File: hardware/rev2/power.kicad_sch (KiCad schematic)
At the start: 19 parts, among them J8 Battery Connection, U5 MP2664GG-xxxx-P, U6 MAX17055ETB+, U8 TPS631000DRLR

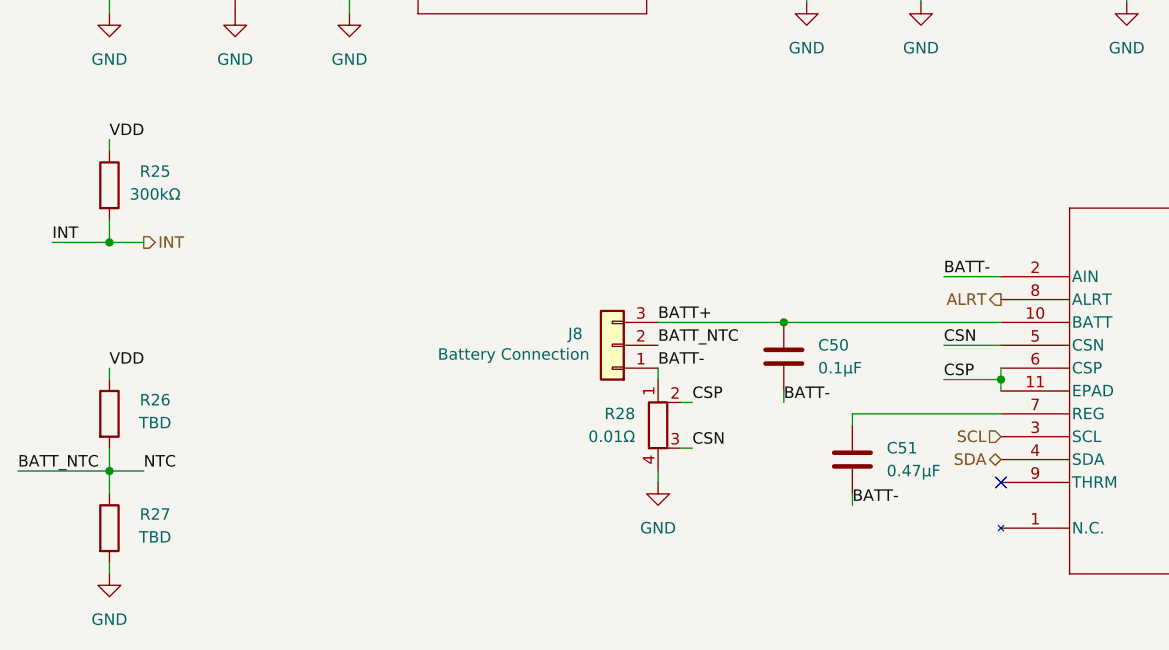
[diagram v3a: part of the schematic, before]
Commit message: Started power system layout
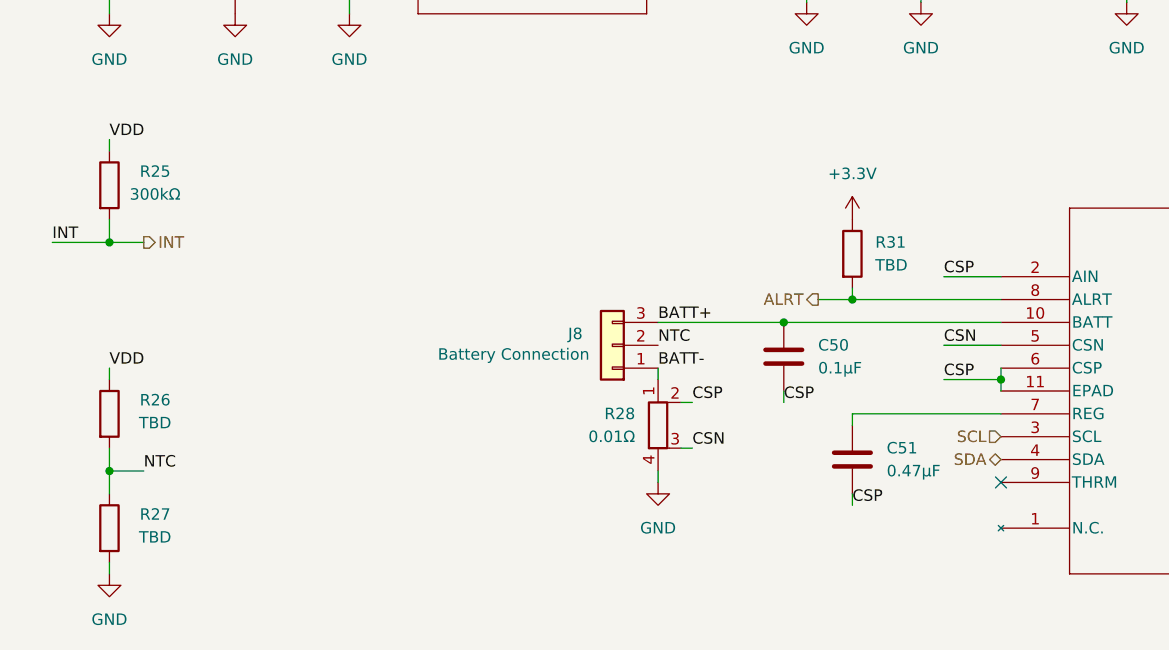
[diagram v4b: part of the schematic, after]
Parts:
- added R31: TBD, Resistor_SMD:R_0603_1608Metric_Pad0.98x0.95mm_HandSolder, symbol Device:R
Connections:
- net +3.3V: now also R31.1
- net ALRT: now also R31.2
- net BATT-: no longer C50.2, C51.2, U6.2 (AIN)
- net CSP: now also C50.2, C51.2, U6.2 (AIN)
- net BATT_NTC renamed NTC
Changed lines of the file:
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@@
 	)
 	(junction
+		(at 120.65 121.92)
+		(diameter 0)
+		(color 0 0 0 0)
+	)
+	(junction
 		(at 38.1 74.93)
 		(diameter 0)
@@
 	(wire
 		(pts
+			(xy 116.84 121.92) (xy 120.65 121.92)
+		)
+		(stroke
+			(width 0)
+			(type default)
+		)
+	)
+	(wire
+		(pts
 			(xy 38.1 143.51) (xy 38.1 140.97)
 		)
@@
 	(wire
 		(pts
-			(xy 113.03 133.35) (xy 113.03 132.08)
+			(xy 120.65 121.92) (xy 137.16 121.92)
 		)
 		(stroke
@@
 	(wire
 		(pts
-			(xy 156.21 72.39) (xy 162.56 72.39)
+			(xy 113.03 133.35) (xy 113.03 132.08)
 		)
 		(stroke
@@
 	(wire
 		(pts
-			(xy 130.81 127) (xy 137.16 127)
+			(xy 156.21 72.39) (xy 162.56 72.39)
 		)
 		(stroke
@@
 	(wire
 		(pts
-			(xy 128.27 74.93) (xy 151.13 74.93)
+			(xy 130.81 127) (xy 137.16 127)
 		)
 		(stroke
@@
 	(wire
 		(pts
-			(xy 38.1 140.97) (xy 41.91 140.97)
+			(xy 128.27 74.93) (xy 151.13 74.93)
 		)
 		(stroke
@@
 	(wire
 		(pts
-			(xy 27.94 140.97) (xy 38.1 140.97)
+			(xy 38.1 140.97) (xy 41.91 140.97)
 		)
 		(stroke
@@
 	(wire
 		(pts
+			(xy 120.65 120.65) (xy 120.65 121.92)
+		)
+		(stroke
+			(width 0)
+			(type default)
+		)
+	)
+	(wire
+		(pts
 			(xy 199.39 53.34) (xy 162.56 53.34)
 		)
@@
 		)
 	)
-	(label "BATT-"
+	(label "CSP"
 		(at 120.65 144.78 0)
 		(effects
@@
 		)
 	)
-	(label "BATT_NTC"
-		(at 27.94 140.97 0)
-		(effects
-			(font
-				(size 1.27 1.27)
-			)
-			(justify left bottom)
-		)
-	)
 	(label "BATT-"
 		(at 99.06 129.54 0)
@@
 		)
 	)
-	(label "BATT-"
+	(label "CSP"
 		(at 113.03 133.35 0)
 		(effects
@@
 		)
 	)
-	(label "BATT_NTC"
+	(label "NTC"
 		(at 99.06 127 0)
 		(effects
@@
 		)
 	)
-	(label "BATT-"
+	(label "CSP"
 		(at 130.81 119.38 0)
 		(effects
@@
 	(hierarchical_label "ALRT"
 		(shape output)
-		(at 137.16 121.92 180)
+		(at 116.84 121.92 180)
 		(effects
 			(font
@@
 	)
 	(symbol
+		(lib_id "power:+3.3V")
+		(at 120.65 113.03 0)
+		(unit 1)
+		(body_style 1)
+		(exclude_from_sim no)
+		(in_bom yes)
+		(on_board yes)
+		(in_pos_files yes)
+		(dnp no)
+		(fields_autoplaced yes)
+		(property "Reference" "#PWR087"
+			(at 120.65 116.84 0)
+			(hide yes)
+			(show_name no)
+			(do_not_autoplace no)
+			(effects
+				(font
+					(size 1.27 1.27)
+				)
+			)
+		)
+		(property "Value" "+3.3V"
+			(at 120.65 107.95 0)
+			(show_name no)
+			(do_not_autoplace no)
+			(effects
+				(font
+					(size 1.27 1.27)
+				)
+			)
+		)
+		(property "Footprint" ""
+			(at 120.65 113.03 0)
+			(hide yes)
+			(show_name no)
+			(do_not_autoplace no)
+			(effects
+				(font
+					(size 1.27 1.27)
+				)
+			)
+		)
+		(property "Datasheet" ""
+			(at 120.65 113.03 0)
+			(hide yes)
+			(show_name no)
+			(do_not_autoplace no)
+			(effects
+				(font
+					(size 1.27 1.27)
+				)
+			)
+		)
+		(property "Description" "Power symbol creates a global label with name \"+3.3V\""
+			(at 120.65 113.03 0)
+			(hide yes)
+			(show_name no)
+			(do_not_autoplace no)
+			(effects
+				(font
+					(size 1.27 1.27)
+				)
+			)
+		)
+		(pin "1"
+		)
+		(instances
+			(project "rev2"
+				(path "/9067f306-e23c-4d77-8182-4fa2c4b88902/46484475-7656-401a-9d45-159f5e421427"
+					(reference "#PWR087")
+					(unit 1)
+				)
+			)
+		)
+	)
+	(symbol
 		(lib_id "power:GND")
 		(at 64.77 90.17 0)
@@
 					(unit 1)
 				)
+			)
+		)
+	)
+	(symbol
+		(lib_id "Device:R")
+		(at 120.65 116.84 0)
+		(unit 1)
+		(body_style 1)
+		(exclude_from_sim no)
+		(in_bom yes)
+		(on_board yes)
+		(in_pos_files yes)
+		(dnp no)
+		(property "Reference" "R31"
+			(at 123.19 115.5699 0)
+			(show_name no)
+			(do_not_autoplace no)
+			(effects
+				(font
+					(size 1.27 1.27)
+				)
+				(justify left)
+			)
+		)
+		(property "Value" "TBD"
+			(at 123.19 118.11 0)
+			(show_name no)
+			(do_not_autoplace no)
+			(effects
+				(font
+					(size 1.27 1.27)
+				)
+				(justify left)
+			)
+		)
+		(property "Footprint" "Resistor_SMD:R_0603_1608Metric_Pad0.98x0.95mm_HandSolder"
+			(at 118.872 116.84 90)
+			(hide yes)
+			(show_name no)
+			(do_not_autoplace no)
+			(effects
+				(font
+					(size 1.27 1.27)
+				)
+			)
+		)
+		(property "Datasheet" ""
+			(at 120.65 116.84 0)
+			(hide yes)
+			(show_name no)
+			(do_not_autoplace no)
+			(effects
+				(font
+					(size 1.27 1.27)
+				)
+			)
+		)
+		(property "Description" "Resistor"
+			(at 120.65 116.84 0)
+			(hide yes)
+			(show_name no)
+			(do_not_autoplace no)
+			(effects
+				(font
+					(size 1.27 1.27)
+				)
+			)
+		)
+		(pin "1"
+		)
+		(pin "2"
+		)
+		(instances
+			(project "rev2"
+				(path "/9067f306-e23c-4d77-8182-4fa2c4b88902/46484475-7656-401a-9d45-159f5e421427"
+					(reference "R31")
+					(unit 1)
+				)

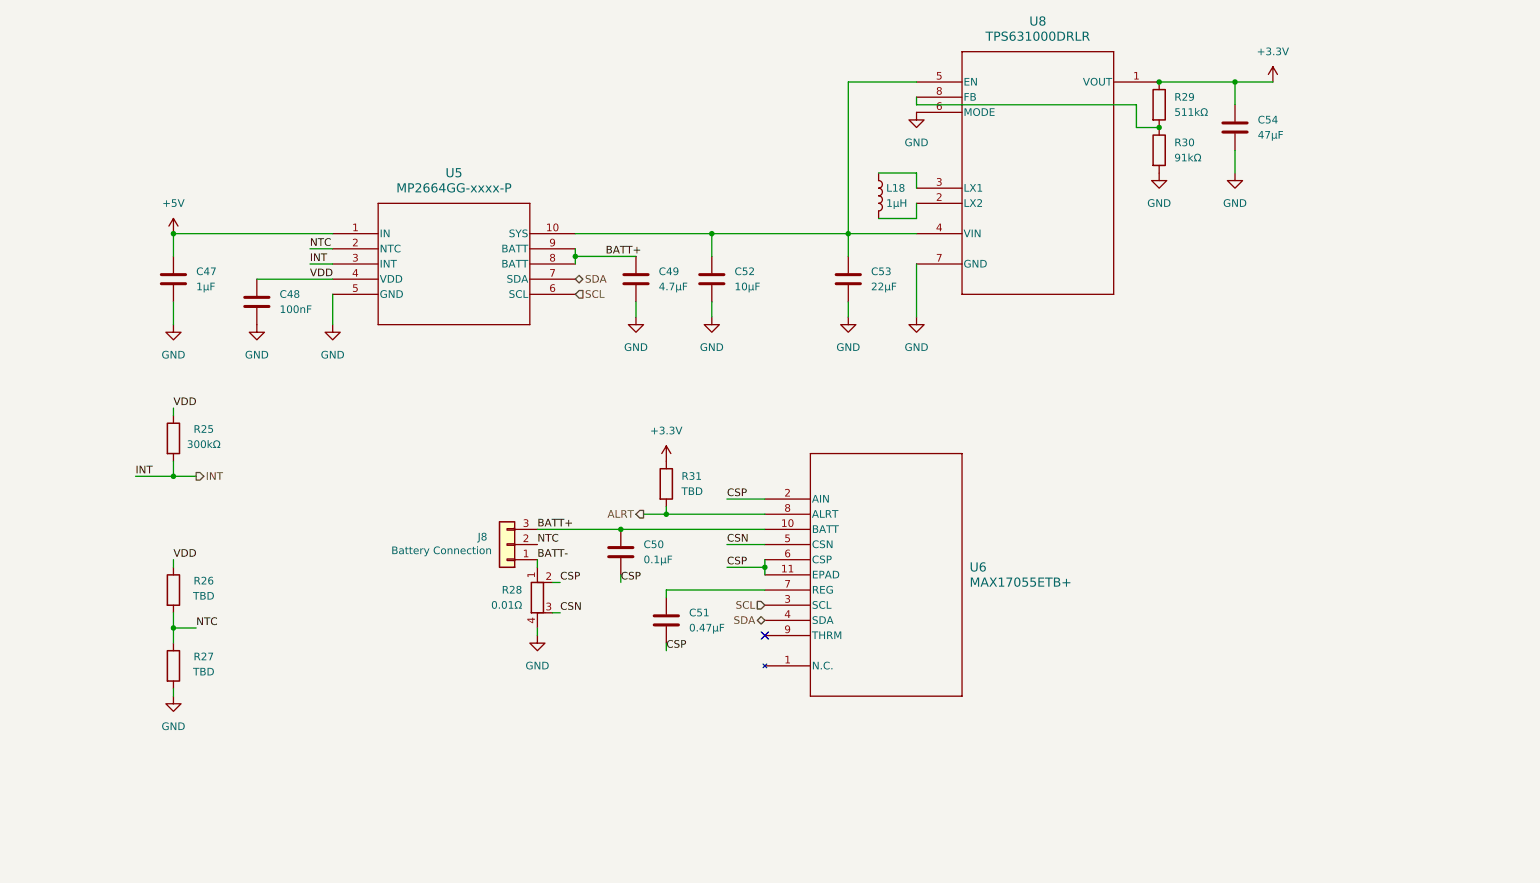
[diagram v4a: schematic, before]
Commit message: added testpoints, added LEDs, fixed a lot of DRC stuff
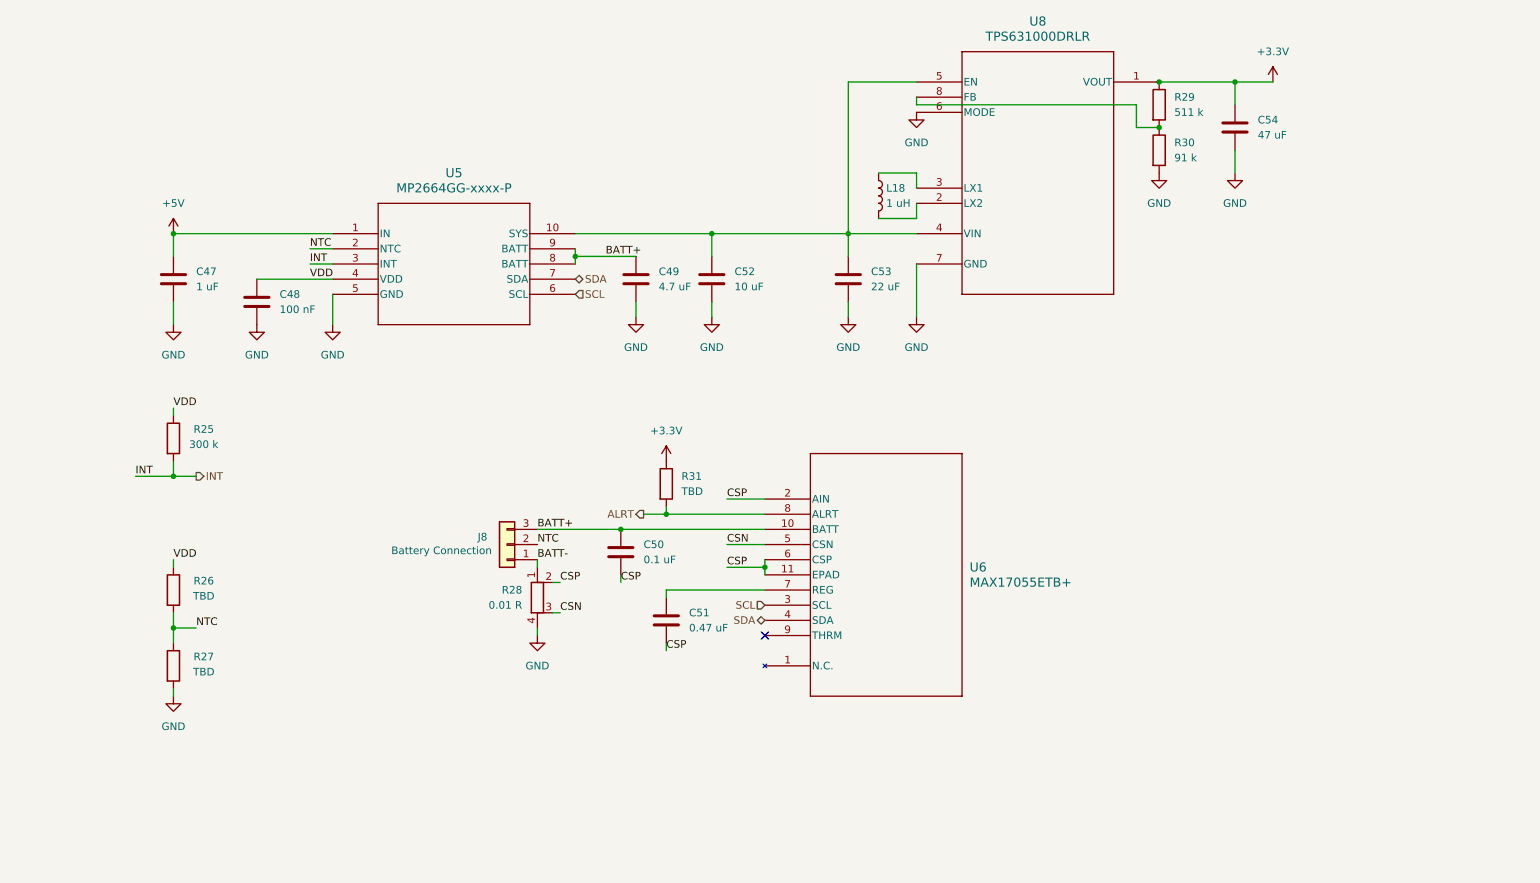
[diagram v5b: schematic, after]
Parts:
- C47: value 1µF -> 1 uF; Mouser Part Number (none) -> 81-GRM188R61C105KA2J
- C48: value 100nF -> 100 nF
- C49: value 4.7µF -> 4.7 uF
- C50: value 0.1µF -> 0.1 uF; Mouser Part Number (none) -> 81-GCJ188R71E104KA2D
- C51: value 0.47µF -> 0.47 uF
- C52: value 10µF -> 10 uF; Mouser Part Number (none) -> 81-GRM188D70J106MA3D
- C53: value 22µF -> 22 uF
- C54: value 47µF -> 47 uF
- L18: value 1µH -> 1 uH
- R25: value 300kΩ -> 300 k
- R28: value 0.01Ω -> 0.01 R
- R29: value 511kΩ -> 511 k
- R30: value 91kΩ -> 91 k
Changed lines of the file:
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@@
 			)
 		)
-		(property "Value" "511kΩ"
+		(property "Value" "511 k"
 			(at 205.74 54.6099 0)
 			(show_name no)
@@
 			)
 		)
-		(property "Value" "0.47µF"
+		(property "Value" "0.47 uF"
 			(at 124.46 140.97 0)
 			(show_name no)
@@
 			)
 		)
-		(property "Value" "47µF"
+		(property "Value" "47 uF"
 			(at 219.71 58.4199 0)
 			(show_name no)
@@
 			)
 		)
-		(property "Value" "22µF"
+		(property "Value" "22 uF"
 			(at 154.94 83.8199 0)
 			(show_name no)
@@
 			)
 		)
-		(property "Value" "91kΩ"
+		(property "Value" "91 k"
 			(at 205.74 62.2299 0)
 			(show_name no)
@@
 			)
 		)
-		(property "Value" "100nF"
+		(property "Value" "100 nF"
 			(at 55.88 87.6299 0)
 			(show_name no)
@@
 			)
 		)
-		(property "Value" "4.7µF"
+		(property "Value" "4.7 uF"
 			(at 119.38 83.8199 0)
 			(show_name no)
@@
 			)
 		)
-		(property "Value" "0.1µF"
+		(property "Value" "0.1 uF"
 			(at 116.84 129.5399 0)
 			(show_name no)
@@
 			)
 		)
-		(property "Datasheet" ""
+		(property "Datasheet" "https://www.mouser.se/datasheet/3/76/1/GCJ188R71E104KA12_02B.pdf"
 			(at 113.03 128.27 0)
 			(hide yes)
@@
 			)
 		)
+		(property "Mouser Part Number" "81-GCJ188R71E104KA2D "
+			(at 113.03 128.27 0)
+			(hide yes)
+			(show_name no)
+			(do_not_autoplace no)
+			(effects
+				(font
+					(size 1.27 1.27)
+				)
+			)
+		)
 		(pin "1"
 		)
@@
 			)
 		)
-		(property "Value" "300kΩ"
+		(property "Value" "300 k"
 			(at 43.18 110.236 0)
 			(show_name no)
@@
 			)
 		)
-		(property "Value" "10µF"
+		(property "Value" "10 uF"
 			(at 132.08 83.8199 0)
 			(show_name no)
@@
 			)
 		)
-		(property "Datasheet" ""
+		(property "Datasheet" "https://pim.murata.com/asset/pim4/ceramicCapacitorSMD/GRM188D70J106MA73-01A-EN_PDF_CERAMICCAPACITORSMD"
 			(at 128.27 82.55 0)
 			(hide yes)
@@
 		)
 		(property "Sim.Type" ""
+			(at 128.27 82.55 0)
+			(hide yes)
+			(show_name no)
+			(do_not_autoplace no)
+			(effects
+				(font
+					(size 1.27 1.27)
+				)
+			)
+		)
+		(property "Mouser Part Number" "81-GRM188D70J106MA3D"
 			(at 128.27 82.55 0)
 			(hide yes)
@@
 			)
 		)
-		(property "Value" "1µH"
+		(property "Value" "1 uH"
 			(at 157.48 69.8499 0)
 			(show_name no)
@@
 			)
 		)
-		(property "Value" "0.01Ω"
+		(property "Value" "0.01 R"
 			(at 96.52 137.1599 0)
 			(show_name no)
@@
 			)
 		)
-		(property "Value" "1µF"
+		(property "Value" "1 uF"
 			(at 41.91 83.8199 0)
 			(show_name no)
@@
 			)
 		)
-		(property "Datasheet" ""
+		(property "Datasheet" "https://pim.murata.com/asset/pim4/ceramicCapacitorSMD/GRM188R61C105KA12-02A-EN_PDF_CERAMICCAPACITORSMD"
 			(at 38.1 82.55 0)
 			(hide yes)
@@
 			(at 38.1 82.55 0)
 			(hide yes)
+			(show_name no)
+			(do_not_autoplace no)
+			(effects
+				(font
+					(size 1.27 1.27)
+				)
+			)
+		)
+		(property "Mouser Part Number" "81-GRM188R61C105KA2J"
+			(at 38.1 82.55 0)
+			(hide yes)

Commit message: Finished power layout
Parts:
- added JP1: Storage mode jumper, Connector_PinHeader_1.00mm:PinHeader_1x03_P1.00mm_Vertical, symbol Jumper:Jumper_3_Bridged12
- added R35: TBD, Resistor_SMD:R_0603_1608Metric_Pad0.98x0.95mm_HandSolder, symbol Device:R
- R28: footprint _footprints:RES_WSK2512R0100FEA -> _footprints:RES_WSK1206R0100FEA; Mouser Part Number 71-WSK2512R0100FEA -> 71-WSK1206R0100FEA
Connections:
- net GND: now also R35.2
- net INT: now also JP1.2 (C); no longer R25.2
- net +3.3V renamed +3V3
- new net: JP1.3 (B), R35.1
- new net: JP1.1 (A), R25.2
- no-connect marks 1 -> 2
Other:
- moved on the sheet: R25, R26, R27
